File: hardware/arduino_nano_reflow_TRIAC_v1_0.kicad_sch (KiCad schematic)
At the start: 34 parts, among them J1 AC IN 220v, J10 CONN_01X17, J11 CONN_01X03, J12 MOUNTING_HOLE, J13 MOUNTING_HOLE, J14 MOUNTING_HOLE, J15 MOUNTING_HOLE, J2 HEATER, J3 DC IN 12V, J4 12v FAN, J5 CONN_01X03, J6 CONN_01X03, J7 CONN_01X03, J8 CONN_01X03, J9 CONN_01X05, Q1 IRF540N, U1 MOC3020M

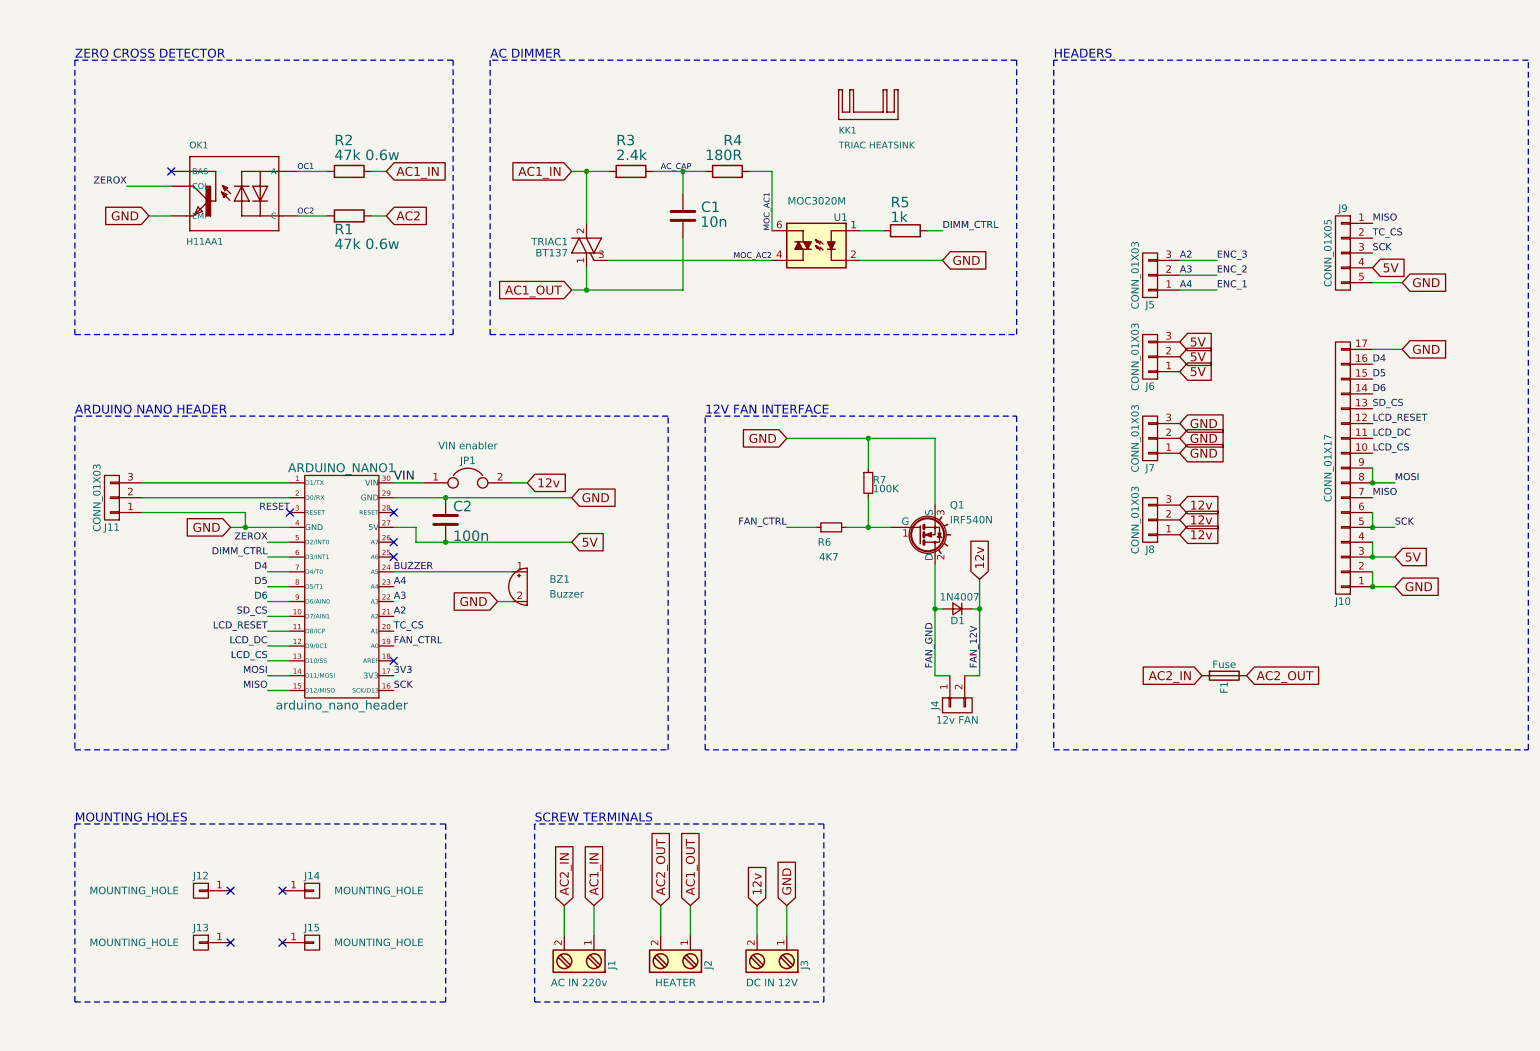
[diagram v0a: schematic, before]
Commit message: Update schematic: Reorganized and added AC power supply.
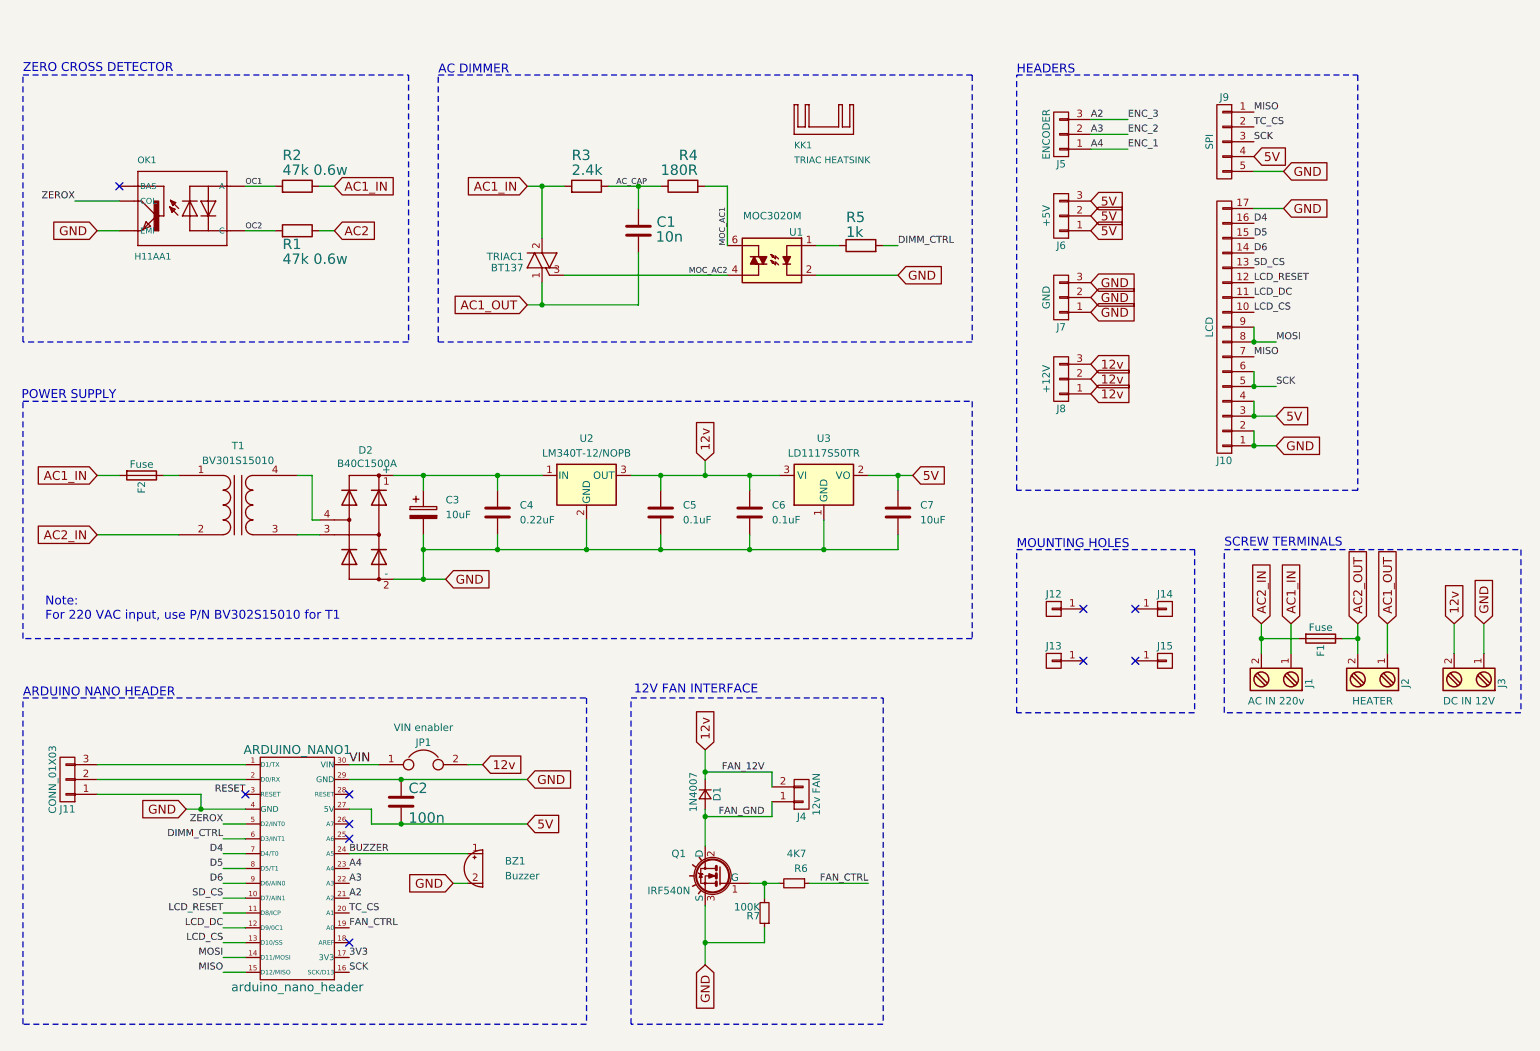
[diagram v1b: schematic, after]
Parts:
- added C3: 10uF, Capacitor_THT:C_Radial_D4.0mm_H7.0mm_P1.50mm, symbol Device:C_Polarized
- added C4: 0.22uF, Capacitor_SMD:C_0805_2012Metric, symbol Device:C
- added C5, C6: 0.1uF, Capacitor_SMD:C_0805_2012Metric, symbol Device:C
- added C7: 10uF, Capacitor_SMD:C_0805_2012Metric, symbol Device:C
- added D2: B40C1500A, symbol bridge_1ph:Bridge_1ph
- added F2: Fuse, Fuse_Holders_and_Fuses:Fuseholder5x20_horiz_open_inline_Type-I, symbol arduino_nano_reflow_TRIAC_v1_0-rescue:Fuse
- added T1: BV301S15010, arduino_nano_reflow:BV301S15010, symbol Device:Transformer_1P_1S
- added U2: LM340T-12/NOPB, symbol arduino_nano_reflow:LM340
- added U3: LD1117S50TR, Package_TO_SOT_SMD:SOT-223-3_TabPin2, symbol Regulator_Linear:LD1117S50TR_SOT223
- J10: value CONN_01X17 -> LCD
- J5: value CONN_01X03 -> ENCODER
- J6: value CONN_01X03 -> +5V
- J7: value CONN_01X03 -> GND
- J8: value CONN_01X03 -> +12V
- J9: value CONN_01X05 -> SPI
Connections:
- net 12v: now also C5.1, C6.1, U2.3 (OUT), U3.3 (VI)
- net 5V: now also C7.1, U3.2 (VO)
- net AC1_IN: now also F2.2
- net AC2_IN: now also T1.2 (AB)
- net GND: now also C3.2, C4.2, C5.2, C6.2, C7.2, D2.2 (-), U2.2 (GND), U3.1 (GND)
- new net: F2.1, T1.1 (AA)
- new net: C3.1, C4.1, D2.1 (+), U2.1 (IN)
- new net: D2.3, T1.3 (SA)
- new net: D2.4, T1.4 (SB)
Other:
- note added: "Note: For 220 VAC input, use P/N BV302S15010 for T1"
- note added: "POWER SUPPLY"
- moved on the sheet: ARDUINO_NANO1, BZ1, C1, C2, D1, F1, J1, J10, J11, J12, J13, J14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

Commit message: Big update. Lots of schematic reorg and mostly final PCB layout. Updated zero crossing detector to be more accurate and added temp sensor on board instead of a connector to a separate module. Moved some pins around on the micro for better layout. Added safety ground to mains input.
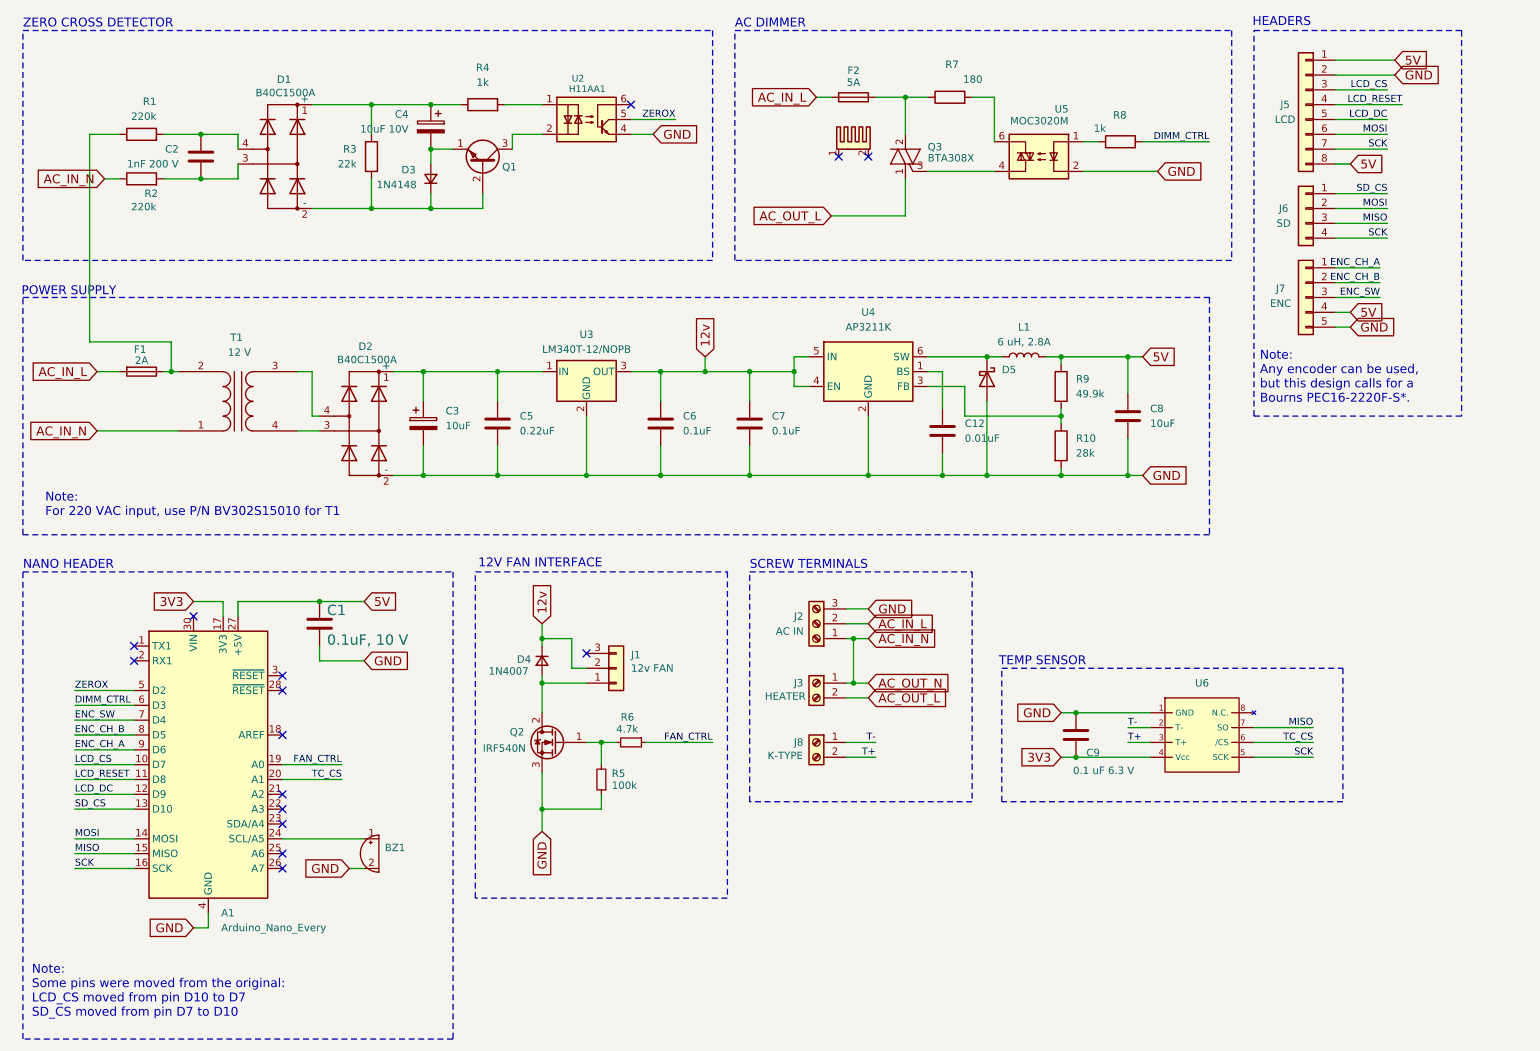
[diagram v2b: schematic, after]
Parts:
- removed ARDUINO_NANO1: arduino_nano_header, local_modules:arduino_nano_header, symbol arduino_nano_reflow_TRIAC_v1_0-rescue:arduino_nano_header
- removed C2: 100n, Capacitors_SMD:C_1206_HandSoldering, symbol arduino_nano_reflow_TRIAC_v1_0-rescue:C
- removed J10: LCD, Pin_Headers:Pin_Header_Straight_1x17_Pitch2.54mm, symbol arduino_nano_reflow_TRIAC_v1_0-rescue:CONN_01X17
- removed J11: CONN_01X03, Pin_Headers:Pin_Header_Straight_1x03_Pitch2.54mm, symbol arduino_nano_reflow_TRIAC_v1_0-rescue:CONN_01X03
- removed J12, J13, J14, J15: MOUNTING_HOLE, Mounting_Holes:MountingHole_3.2mm_M3_Pad_Via, symbol arduino_nano_reflow_TRIAC_v1_0-rescue:CONN_01X01
- removed J3: DC IN 12V, Connectors_Terminal_Blocks:TerminalBlock_Pheonix_MKDS1.5-2pol, symbol arduino_nano_reflow_TRIAC_v1_0-rescue:Screw_Terminal_1x02
- removed J6: +5V, Pin_Headers:Pin_Header_Straight_1x03_Pitch2.54mm, symbol arduino_nano_reflow_TRIAC_v1_0-rescue:CONN_01X03
- removed J7: GND, Pin_Headers:Pin_Header_Straight_1x03_Pitch2.54mm, symbol arduino_nano_reflow_TRIAC_v1_0-rescue:CONN_01X03
- removed J8: +12V, Pin_Headers:Pin_Header_Straight_1x03_Pitch2.54mm, symbol arduino_nano_reflow_TRIAC_v1_0-rescue:CONN_01X03
- removed J9: SPI, Pin_Headers:Pin_Header_Straight_1x05_Pitch2.54mm, symbol arduino_nano_reflow_TRIAC_v1_0-rescue:CONN_01X05
- removed JP1: VIN enabler, Pin_Headers:Pin_Header_Straight_1x02_Pitch2.54mm, symbol arduino_nano_reflow_TRIAC_v1_0-rescue:Jumper
- removed KK1: TRIAC HEATSINK, local_modules:SK_09_20_SA_TO_220, symbol arduino_nano_reflow_TRIAC_v1_0-rescue:SK_09_20_SA_TO_220
- removed R3: 2.4k, Resistors_THT:R_Axial_DIN0207_L6.3mm_D2.5mm_P7.62mm_Horizontal, symbol arduino_nano_reflow_TRIAC_v1_0-rescue:R
- removed U3: LD1117S50TR, Package_TO_SOT_SMD:SOT-223-3_TabPin2, symbol Regulator_Linear:LD1117S50TR_SOT223
- added A1: Arduino_Nano_Every, Module:Arduino_Nano, symbol MCU_Module:Arduino_Nano_Every
- added C12: 0.01uF, Capacitor_SMD:C_0805_2012Metric_Pad1.18x1.45mm_HandSolder, symbol Device:C
- added C2: 1nF 200 V, Capacitor_THT:C_Rect_L7.2mm_W2.5mm_P5.00mm_FKS2_FKP2_MKS2_MKP2, symbol Device:C
- added C4: 10uF 10V, Capacitor_THT:CP_Radial_D5.0mm_P2.00mm, symbol Device:C_Polarized
- added C9: 0.1 uF 6.3 V, Capacitor_SMD:C_0805_2012Metric_Pad1.18x1.45mm_HandSolder, symbol Device:C
- added D1: B40C1500A, arduino_nano_reflow:B40C, symbol bridge_1ph:Bridge_1ph
- added D3: 1N4148, Diode_THT:D_DO-35_SOD27_P7.62mm_Horizontal, symbol Device:D_Small
- added D5: 40V, 2A, Diode_SMD:D_SMA_Handsoldering, symbol Device:D_Schottky
- added HS1: ~, arduino_nano_reflow:Aavid 51300 Heatsink, symbol Mechanical:Heatsink_Pad_2Pin
- added J5: LCD, Connector_PinHeader_2.54mm:PinHeader_1x08_P2.54mm_Vertical, symbol Connector_Generic:Conn_01x08
- added J6: SD, Connector_PinHeader_2.54mm:PinHeader_1x04_P2.54mm_Vertical, symbol Connector_Generic:Conn_01x04
- added J8: K-TYPE, TerminalBlock_Phoenix:TerminalBlock_Phoenix_MKDS-1,5-2_1x02_P5.00mm_Horizontal, symbol Connector:Screw_Terminal_01x02
- added L1: 6 uH, 2.8A, arduino_nano_reflow:Bourns SRN6028C Inductor hand solder, symbol Device:L
- added Q1: 40V, 0.8A, Package_TO_SOT_THT:TO-92_Inline_Wide, symbol Transistor_BJT:PN2222A
- added R10: 28k, Resistor_SMD:R_0805_2012Metric_Pad1.20x1.40mm_HandSolder, symbol Device:R
- added R3: 22k, Resistor_THT:R_Axial_DIN0204_L3.6mm_D1.6mm_P5.08mm_Horizontal, symbol Device:R
- added R4: 1k, Resistor_THT:R_Axial_DIN0204_L3.6mm_D1.6mm_P5.08mm_Horizontal, symbol Device:R
- added R9: 49.9k, Resistor_SMD:R_0805_2012Metric_Pad1.20x1.40mm_HandSolder, symbol Device:R
- added U4: AP3211K, Package_TO_SOT_SMD:SOT-23-6_Handsoldering, symbol Regulator_Switching:AP3211K
- added U6: ~, Package_SO:SO-8_3.9x4.9mm_P1.27mm, symbol arduino_nano_reflow:MAX6675
- BZ1: value Buzzer -> ~; footprint Buzzers_Beepers:Buzzer_12x9.5RM7.6 -> Buzzer_Beeper:Buzzer_TDK_PS1240P02BT_D12.2mm_H6.5mm; Manufacturer (none) -> Soberton; Part Number (none) -> WT-1205
- C1: value 10n -> 0.1uF, 10 V; footprint Capacitors_THT:C_Disc_D4.3mm_W1.9mm_P5.00mm -> Capacitor_SMD:C_0805_2012Metric_Pad1.18x1.45mm_HandSolder; Manufacturer (none) -> Kemet; Part Number (none) -> C0805C104K8RACTU
- C3: footprint Capacitor_THT:C_Radial_D4.0mm_H7.0mm_P1.50mm -> Capacitor_THT:CP_Radial_D5.0mm_P2.00mm; Manufacturer (none) -> Kemet
- C5: renamed from C4; footprint Capacitor_SMD:C_0805_2012Metric -> Capacitor_SMD:C_0805_2012Metric_Pad1.18x1.45mm_HandSolder; Manufacturer (none) -> Kemet
- C6: renamed from C5; footprint Capacitor_SMD:C_0805_2012Metric -> Capacitor_SMD:C_0805_2012Metric_Pad1.18x1.45mm_HandSolder; Manufacturer (none) -> Kemet
- C7: renamed from C6; footprint Capacitor_SMD:C_0805_2012Metric -> Capacitor_SMD:C_0805_2012Metric_Pad1.18x1.45mm_HandSolder; Manufacturer (none) -> Kemet
- C8: renamed from C7; footprint Capacitor_SMD:C_0805_2012Metric -> Capacitor_SMD:C_0805_2012Metric_Pad1.18x1.45mm_HandSolder; Manufacturer (none) -> Kemet; Part Number (none) -> C0805C106K9PACTU
- D2: footprint (none) -> arduino_nano_reflow:B40C; Manufacturer (none) -> Diotec; Part Number (none) -> B40C1500A
- D4: renamed from D1; footprint Diodes_THT:D_A-405_P5.08mm_Vertical_AnodeUp -> Diode_THT:D_DO-35_SOD27_P7.62mm_Horizontal; symbol arduino_nano_reflow_TRIAC_v1_0-rescue:D_Small -> Device:D_Small; Manufacturer (none) -> Diotec; Part Number (none) -> 1N4007
- F1: renamed from F2; value Fuse -> 2A; footprint Fuse_Holders_and_Fuses:Fuseholder5x20_horiz_open_inline_Type-I -> arduino_nano_reflow:FUSE_0PTF0078P_LTF; symbol arduino_nano_reflow_TRIAC_v1_0-rescue:Fuse -> Device:Fuse; Manufacturer (none) -> Littelfuse; Part Number (none) -> 0PTF0078P
- F2: renamed from F1; value Fuse -> 5A; footprint Fuse_Holders_and_Fuses:Fuseholder5x20_horiz_open_inline_Type-I -> arduino_nano_reflow:FUSE_0PTF0078P_LTF; symbol arduino_nano_reflow_TRIAC_v1_0-rescue:Fuse -> Device:Fuse; Manufacturer (none) -> Littelfuse; Part Number (none) -> 0PTF0078P
- J1: renamed from J4; footprint Pin_Headers:Pin_Header_Straight_2x01_Pitch2.54mm -> Connector:FanPinHeader_1x03_P2.54mm_Vertical; symbol arduino_nano_reflow_TRIAC_v1_0-rescue:CONN_01X02 -> Connector_Generic:Conn_01x03; Manufacturer (none) -> TE Connectivity; Part Number (none) -> 640456-3
- J2: renamed from J1; value AC IN 220v -> AC IN; footprint Connectors_Terminal_Blocks:TerminalBlock_Pheonix_MKDS1.5-2pol -> TerminalBlock_Phoenix:TerminalBlock_Phoenix_MKDS-1,5-3_1x03_P5.00mm_Horizontal; symbol arduino_nano_reflow_TRIAC_v1_0-rescue:Screw_Terminal_1x02 -> Connector:Screw_Terminal_01x03; Manufacturer (none) -> Phoenix; Part Number (none) -> 1727023
- J3: renamed from J2; footprint Connectors_Terminal_Blocks:TerminalBlock_Pheonix_MKDS1.5-2pol -> TerminalBlock_Phoenix:TerminalBlock_Phoenix_MKDS-1,5-2_1x02_P5.00mm_Horizontal; symbol arduino_nano_reflow_TRIAC_v1_0-rescue:Screw_Terminal_1x02 -> Connector:Screw_Terminal_01x02; Manufacturer (none) -> Phoenix; Part Number (none) -> 1727010
- J7: renamed from J5; value ENCODER -> ENC; footprint Pin_Headers:Pin_Header_Straight_1x03_Pitch2.54mm -> Connector_PinHeader_2.54mm:PinHeader_1x05_P2.54mm_Vertical; symbol arduino_nano_reflow_TRIAC_v1_0-rescue:CONN_01X03 -> Connector_Generic:Conn_01x05; Manufacturer (none) -> Harwin Inc; Part Number (none) -> M20-9990546
- Q2: renamed from Q1; footprint TO_SOT_Packages_THT:TO-220_Vertical -> Package_TO_SOT_THT:TO-220-3_Vertical; symbol arduino_nano_reflow_TRIAC_v1_0-rescue:IRF540N -> Transistor_FET:IRF540N; Manufacturer (none) -> International Rectifier; Part Number (none) -> IRF540N
- Q3: renamed from TRIAC1; value BT137 -> BTA308X; footprint local_modules:TO-220_Vertical_BT137 -> Package_TO_SOT_THT:TO-220-3_Vertical; Manufacturer (none) -> WeEn Semiconductor; Part Number (none) -> BTA308X
- R1: renamed from R2; value 47k 0.6w -> 220k; footprint Resistors_THT:R_Axial_DIN0207_L6.3mm_D2.5mm_P7.62mm_Horizontal -> Resistor_THT:R_Axial_DIN0204_L3.6mm_D1.6mm_P5.08mm_Horizontal; symbol arduino_nano_reflow_TRIAC_v1_0-rescue:R -> Device:R; Manufacturer (none) -> Stackpole; Part Number (none) -> CF18JT220K
- R2: renamed from R1; value 47k 0.6w -> 220k; footprint Resistors_THT:R_Axial_DIN0207_L6.3mm_D2.5mm_P7.62mm_Horizontal -> Resistor_THT:R_Axial_DIN0204_L3.6mm_D1.6mm_P5.08mm_Horizontal; symbol arduino_nano_reflow_TRIAC_v1_0-rescue:R -> Device:R; Manufacturer (none) -> Stackpole; Part Number (none) -> CF18JT220K
- R5: renamed from R7; value 100K -> 100k; footprint Resistors_SMD:R_1206_HandSoldering -> Resistor_THT:R_Axial_DIN0204_L3.6mm_D1.6mm_P5.08mm_Horizontal; symbol arduino_nano_reflow_TRIAC_v1_0-rescue:R_Small -> Device:R_Small; Manufacturer (none) -> Stackpole; Part Number (none) -> CF18JT100K
- R6: value 4K7 -> 4.7k; footprint Resistors_THT:R_Axial_DIN0309_L9.0mm_D3.2mm_P12.70mm_Horizontal -> Resistor_THT:R_Axial_DIN0204_L3.6mm_D1.6mm_P5.08mm_Horizontal; symbol arduino_nano_reflow_TRIAC_v1_0-rescue:R_Small -> Device:R_Small; Manufacturer (none) -> Stackpole; Part Number (none) -> CF18JT4K70
- R7: renamed from R4; value 180R -> 180; footprint Resistors_THT:R_Axial_DIN0207_L6.3mm_D2.5mm_P7.62mm_Horizontal -> Resistor_THT:R_Axial_DIN0207_L6.3mm_D2.5mm_P7.62mm_Horizontal; symbol arduino_nano_reflow_TRIAC_v1_0-rescue:R -> Device:R; Manufacturer (none) -> Stackpole; Part Number (none) -> CF18JT180R
- R8: renamed from R5; footprint Resistors_THT:R_Axial_DIN0207_L6.3mm_D2.5mm_P7.62mm_Horizontal -> Resistor_THT:R_Axial_DIN0204_L3.6mm_D1.6mm_P5.08mm_Horizontal; symbol arduino_nano_reflow_TRIAC_v1_0-rescue:R -> Device:R; Manufacturer (none) -> Stackpole; Part Number (none) -> CF18JT1K00
- T1: value BV301S15010 -> 12 V; Manufacturer (none) -> Zettler Magnetics; Part Number (none) -> BV301S15010
- U2: renamed from OK1; footprint Housings_DIP:DIP-6_W7.62mm_LongPads -> Package_DIP:DIP-6_W7.62mm; symbol arduino_nano_reflow_TRIAC_v1_0-rescue:H11AA1 -> Isolator:H11AA1; Manufacturer (none) -> Vishay; Part Number (none) -> H11AA1
- U3: renamed from U2; footprint (none) -> Package_TO_SOT_SMD:TO-263-3_TabPin4; Manufacturer (none) -> Texas Instruments; Part Number (none) -> LM340T-12/NOPB
- U5: renamed from U1; footprint Housings_DIP:DIP-6_W7.62mm_LongPads -> Package_DIP:DIP-6_W7.62mm_Socket_LongPads; symbol arduino_nano_reflow_TRIAC_v1_0-rescue:MOC3020M -> Relay_SolidState:MOC3020M; Manufacturer (none) -> ON Semiconductor; Part Number (none) -> MOC3020M
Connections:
- net 12v: now also U4.4 (EN), U4.5 (IN)
- net 3V3: now also A1.17 (3V3), C9.2, U6.4 (Vcc)
- net 5V: now also C1.1, J7.4 (Pin_4), A1.27 (+5V), J5.1 (Pin_1), J5.8 (Pin_8), L1.2, R9.1
- net DIMM_CTRL: now also A1.6 (D3)
- net FAN_CTRL: now also A1.19 (A0)
- net GND: now also C1.2, J2.3 (Pin_3), J7.5 (Pin_5), A1.29 (GND), A1.4 (GND), C12.2, C9.1, D5.2 (A), J5.2 (Pin_2), R10.2, U4.2 (GND), U6.1 (GND)
- net LCD_CS: now also A1.10 (D7), J5.3 (Pin_3)
- net LCD_DC: now also A1.12 (D9), J5.5 (Pin_5)
- net LCD_RESET: now also A1.11 (D8), J5.4 (Pin_4)
- net MISO: now also A1.15 (MISO), J6.3 (Pin_3), U6.7 (SO)
- net MOSI: now also A1.14 (MOSI), J5.6 (Pin_6), J6.2 (Pin_2)
- net SCK: now also A1.16 (SCK), J5.7 (Pin_7), J6.4 (Pin_4), U6.5 (SCK)
- net SD_CS: now also A1.13 (D10), J6.1 (Pin_1)
- net TC_CS: now also A1.20 (A1), U6.6 (/CS)
- net ZEROX: now also A1.5 (D2)
- net at F1.1: now also R1.1, T1.2 (AB); no longer T1.1 (AA)
- net at T1.3 (SA): now also D2.4; no longer D2.3
- net at T1.4 (SB): now also D2.3; no longer D2.4
- net A2 renamed ENC_SW
- net ENC_SW: now also A1.7 (D4)
- net A3 renamed ENC_CH_B
- net ENC_CH_B: now also A1.8 (D5)
- net A4 renamed ENC_CH_A
- net ENC_CH_A: now also A1.9 (D6)
- removed net AC1_IN: F1.2, J2.1, Q3.2 (A2), R1.1
- removed net AC1_OUT: C1.1, J3.1, Q3.1 (A1)
- net AC2 renamed AC_IN_N
- net AC_IN_N: now also J2.1 (Pin_1), J3.1 (Pin_1), T1.1 (AA)
- removed net AC2_IN: F2.2, J2.2, T1.2 (AB)
- net AC2_OUT renamed AC_IN_L
- net AC_IN_L: now also F1.2, J2.2 (Pin_2); no longer J3.2
- net AC_CAP: no longer names the net of R7.1
- net AC_CAP: now also F2.2, Q3.2 (A2); no longer C1.2
- net BUZZER: no longer names the net of BZ1.1 (-)
- net BUZZER: now also A1.24 (SCL/A5)
- net FAN_GND: no longer names the net of D4.2 (A), J1.1 (Pin_1), Q2.2 (D)
- net MOC_AC1: no longer names the net of R7.2, U5.6
- net MOC_AC2: no longer names the net of Q3.3 (G), U5.4
- net OC1: no longer names the net of R1.2
- net OC1: now also C2.1, D1.4; no longer U2.1 (A)
- net OC2: no longer names the net of R2.2
- net OC2: now also C2.2, D1.3; no longer U2.2 (C)
- new net: R4.2, U2.1
- new net: Q1.3 (C), U2.2
- new net: C4.2, D3.2 (A), Q1.1 (E)
- new net: D1.2 (-), D3.1 (K), Q1.2 (B), R3.2
- new net: D5.1 (K), L1.1, U4.6 (SW)
- new net: C12.1, U4.1 (BS)
- new net: R10.1, R9.2, U4.3 (FB)
- new net: C4.1, D1.1 (+), R3.1, R4.1
- new net AC_OUT_L: J3.2 (Pin_2), Q3.1 (A1)
- new net T+: J8.2 (Pin_2), U6.3 (T+)
- new net T-: J8.1 (Pin_1), U6.2 (T-)
- no-connect marks 10 -> 15
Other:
- note added: "NANO HEADER"
- note added: "Note: Any encoder can be used, but this design calls for a Bourns PEC16-2220F-S*."
- note added: "Note: Some pins were moved from the original: LCD_CS moved from pin D10 to D7 SD_CS moved from pin D7 to D10"
- note added: "TEMP SENSOR"
- note removed: "ARDUINO NANO HEADER"
- note removed: "MOUNTING HOLES"
- company: David Sanz Kirbis -> (none)
- title: Nano Reflow Controller -> Nano Reflow Controller+
- moved on the sheet: C3, C5, C6, C7, C8, D2, D4, F1, F2, J3, Q3, R1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
